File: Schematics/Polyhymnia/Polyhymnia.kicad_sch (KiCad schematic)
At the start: 1 part, among them U1 Teensy4.1

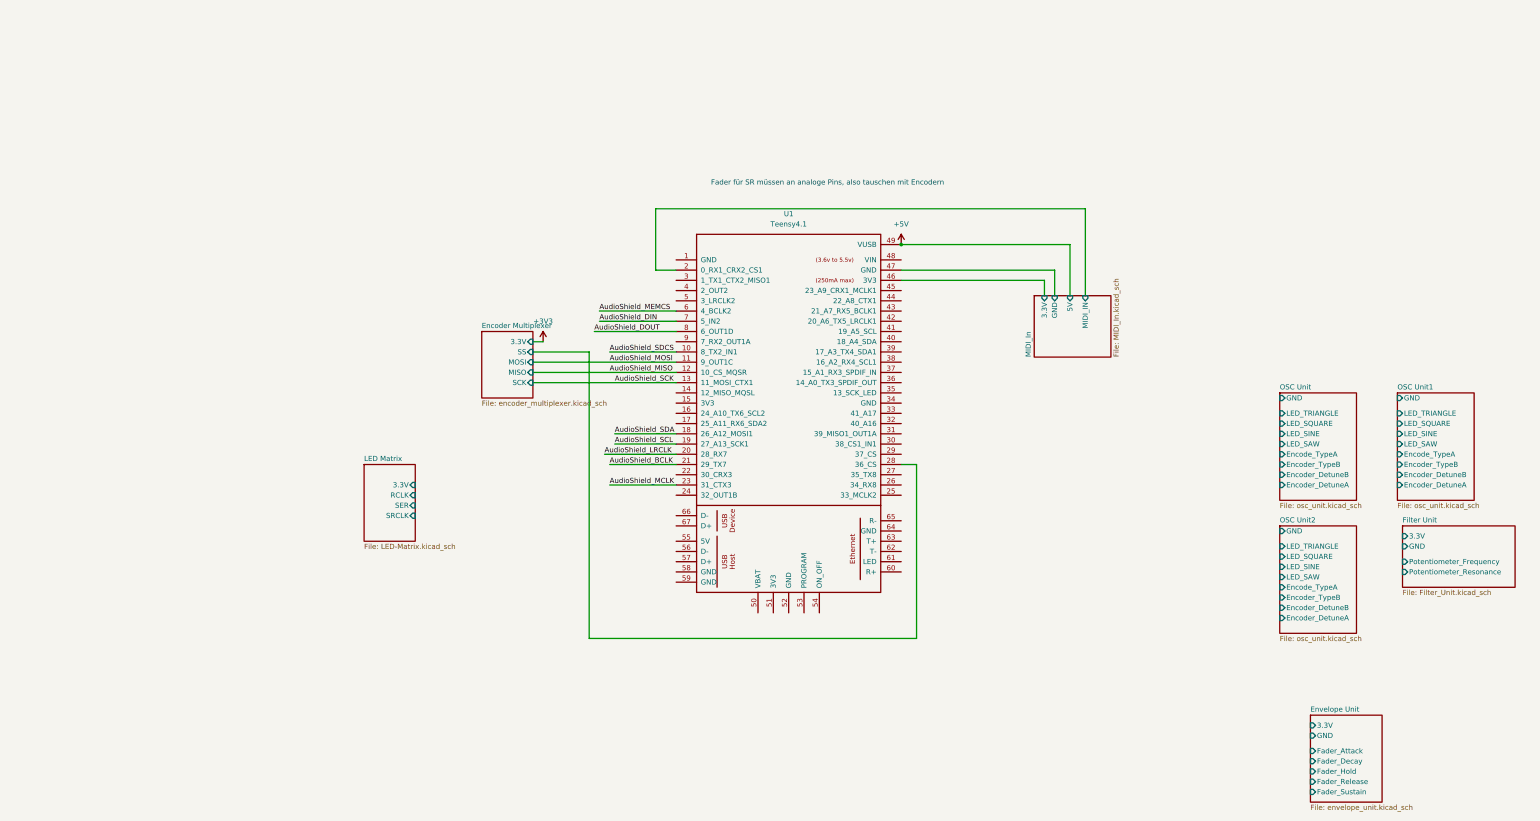
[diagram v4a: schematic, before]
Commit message: Added schematics for OSC, Filter and Envelope and updated README
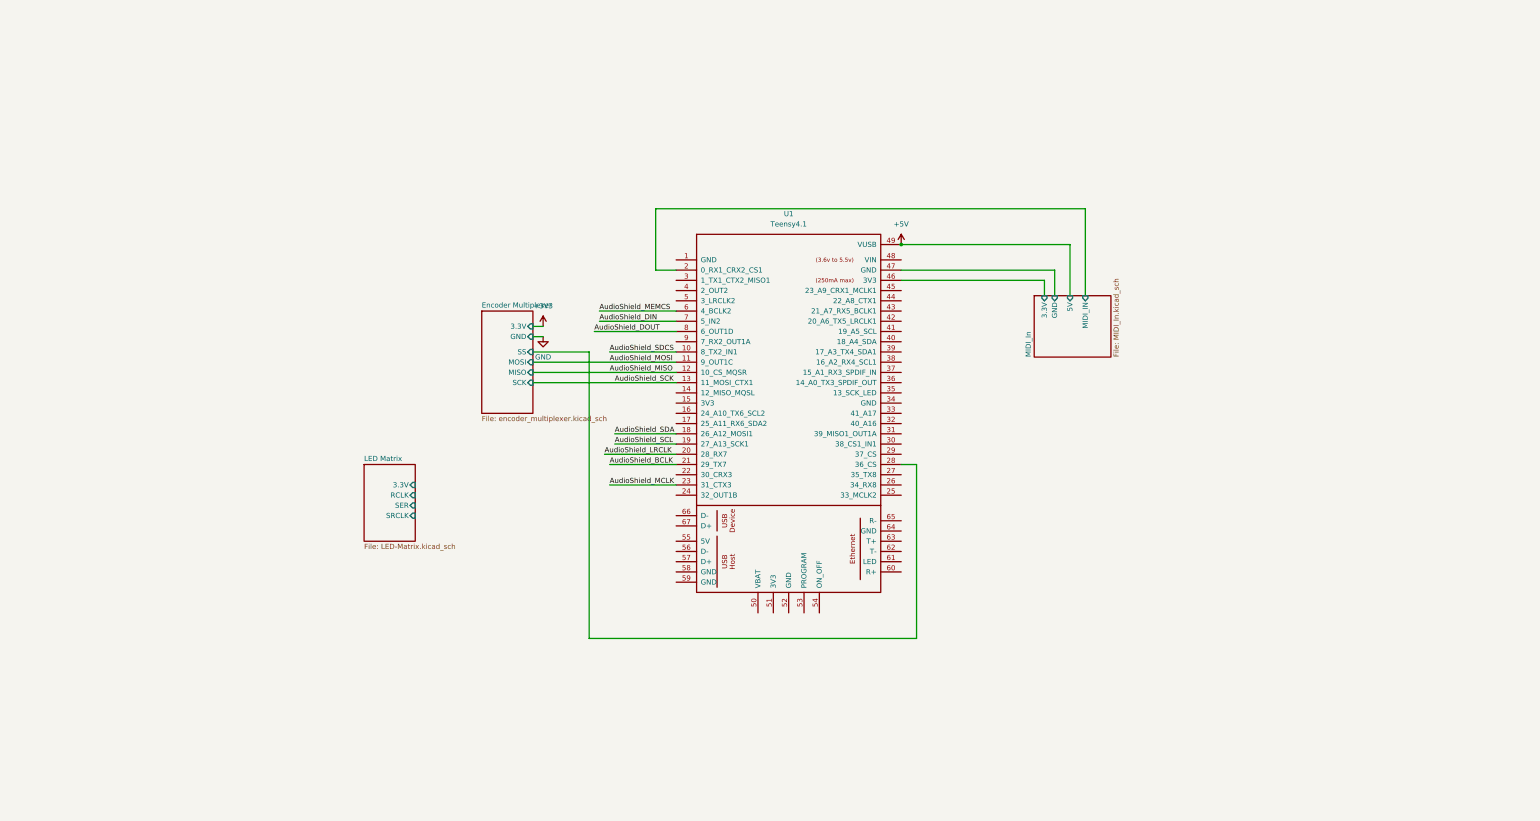
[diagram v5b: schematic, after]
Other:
- removed sheet Envelope Unit
- removed sheet Filter Unit
- removed sheet OSC Unit
- removed sheet OSC Unit1
- removed sheet OSC Unit2
- sheet Encoder Multiplexer ports: added GND; removed none
- note removed: "Fader für SR müssen an analoge Pins, also tauschen mit Encodern"

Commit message: Merge
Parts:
- added R55: 50, symbol Device:R
- added U11: CR2013-MI2120, Display:CR2013-MI2120, symbol Driver_Display:CR2013-MI2120
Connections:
- net AudioShield_DOUT is gone; now on net AudioShield_MEMCS: U1.8 (6_OUT1D)
- net +3V3: now also U11.1 (VCC)
- net AudioShield_BCLK: now also U1.43 (21_A7_RX5_BCLK1); no longer U1.21 (29_TX7)
- net AudioShield_DIN: now also U1.10 (8_TX2_IN1), U1.9 (7_RX2_OUT1A); no longer U1.7 (5_IN2)
- net AudioShield_LRCLK: now also U1.42 (20_A6_TX5_LRCLK1); no longer U1.20 (28_RX7)
- net AudioShield_MCLK: now also U1.45 (23_A9_CRX1_MCLK1); no longer U1.23 (31_CTX3)
- net AudioShield_MEMCS: no longer U1.6 (4_BCLK2)
- net AudioShield_MISO: now also U1.14 (12_MISO_MQSL); no longer U1.12 (10_CS_MQSR)
- net AudioShield_MOSI: now also U1.13 (11_MOSI_CTX1); no longer U1.11 (9_OUT1C)
- net AudioShield_SCK: now also U1.35 (13_SCK_LED); no longer U1.13 (11_MOSI_CTX1)
- net AudioShield_SCL: now also U1.41 (19_A5_SCL); no longer U1.19 (27_A13_SCK1)
- net AudioShield_SDA: now also U1.40 (18_A4_SDA); no longer U1.18 (26_A12_MOSI1)
- net AudioShield_SDCS: now also U1.12 (10_CS_MQSR); no longer U1.10 (8_TX2_IN1)
- net Encoder Multiplexer/SS: no longer U1.28 (36_CS)
- net GND: now also U1.1 (GND), U11.2 (GND)
- net MIDI_In/MIDI_IN: now also U11.5 (D/~{C})
- net at U1.3 (1_TX1_CTX2_MISO1): now also U11.9 (MISO)
- new net: R55.1, U11.8 (LED)
- new net: R55.2, U1.20 (28_RX7)
- new net: U1.21 (29_TX7), U11.4 (RESET)
- new net: U1.18 (26_A12_MOSI1), U11.6 (MOSI)
- new net: U1.19 (27_A13_SCK1), U11.7 (SCK)
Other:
- title: Polyhymnia -> Polyhymnia Main
- moved on the sheet: U1
